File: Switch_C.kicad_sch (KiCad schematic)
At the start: 2 parts

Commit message: progress on CORE pcb
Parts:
- renumbered R801 to R501, R802 to R502
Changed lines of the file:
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@@
 		(on_board yes)
 		(dnp no)
-		(property "Reference" "R801"
+		(property "Reference" "R501"
 			(at 96.52 121.92 0)
 			(effects
@@
 			(project "EPS_CORE"
 				(path "/43e5e7c8-e7e0-4528-9a3e-b1557849918d/170b50a7-486d-470b-9824-bd866624d07a"
-					(reference "R?")
+					(reference "R1501")
 					(unit 1)
 				)
 				(path "/43e5e7c8-e7e0-4528-9a3e-b1557849918d/6ee1dd01-f31d-4eef-845b-d197a7baea1a"
-					(reference "R?")
+					(reference "R1301")
 					(unit 1)
 				)
 				(path "/43e5e7c8-e7e0-4528-9a3e-b1557849918d/7ff03393-ecf4-487d-bab2-a8ed4a4d9be6"
-					(reference "R?")
+					(reference "R701")
 					(unit 1)
 				)
 				(path "/43e5e7c8-e7e0-4528-9a3e-b1557849918d/b6772c72-3c76-48c5-a75b-fb14179eeb30"
-					(reference "R?")
+					(reference "R501")
 					(unit 1)
 				)
@@
 		(on_board yes)
 		(dnp no)
-		(property "Reference" "R802"
+		(property "Reference" "R502"
 			(at 105.41 121.92 0)
 			(effects
@@
 			(project "EPS_CORE"
 				(path "/43e5e7c8-e7e0-4528-9a3e-b1557849918d/170b50a7-486d-470b-9824-bd866624d07a"
-					(reference "R?")
+					(reference "R1502")
 					(unit 1)
 				)
 				(path "/43e5e7c8-e7e0-4528-9a3e-b1557849918d/6ee1dd01-f31d-4eef-845b-d197a7baea1a"
-					(reference "R?")
+					(reference "R1302")
 					(unit 1)
 				)
 				(path "/43e5e7c8-e7e0-4528-9a3e-b1557849918d/7ff03393-ecf4-487d-bab2-a8ed4a4d9be6"
-					(reference "R?")
+					(reference "R702")
 					(unit 1)
 				)
 				(path "/43e5e7c8-e7e0-4528-9a3e-b1557849918d/b6772c72-3c76-48c5-a75b-fb14179eeb30"
-					(reference "R?")
+					(reference "R502")
 					(unit 1)
 				)
@@
 		(dnp no)
 		(fields_autoplaced yes)
-		(property "Reference" "#PWR0165"
+		(property "Reference" "#PWR0164"
 			(at 95.25 132.08 0)
 			(effects
@@
 			(project "EPS_CORE"
 				(path "/43e5e7c8-e7e0-4528-9a3e-b1557849918d/170b50a7-486d-470b-9824-bd866624d07a"
-					(reference "#PWR?")
+					(reference "#PWR0363")
 					(unit 1)
 				)
 				(path "/43e5e7c8-e7e0-4528-9a3e-b1557849918d/6ee1dd01-f31d-4eef-845b-d197a7baea1a"
-					(reference "#PWR?")
+					(reference "#PWR0341")
 					(unit 1)
 				)
 				(path "/43e5e7c8-e7e0-4528-9a3e-b1557849918d/7ff03393-ecf4-487d-bab2-a8ed4a4d9be6"
-					(reference "#PWR?")
+					(reference "#PWR0186")
 					(unit 1)
 				)
 				(path "/43e5e7c8-e7e0-4528-9a3e-b1557849918d/b6772c72-3c76-48c5-a75b-fb14179eeb30"
-					(reference "#PWR?")
+					(reference "#PWR0164")
 					(unit 1)
 				)
@@
 		(dnp no)
 		(fields_autoplaced yes)
-		(property "Reference" "#PWR0166"
+		(property "Reference" "#PWR0165"
 			(at 104.14 132.08 0)
 			(effects
@@
 			(project "EPS_CORE"
 				(path "/43e5e7c8-e7e0-4528-9a3e-b1557849918d/170b50a7-486d-470b-9824-bd866624d07a"
-					(reference "#PWR?")
+					(reference "#PWR0364")
 					(unit 1)
 				)
 				(path "/43e5e7c8-e7e0-4528-9a3e-b1557849918d/6ee1dd01-f31d-4eef-845b-d197a7baea1a"
-					(reference "#PWR?")
+					(reference "#PWR0342")
 					(unit 1)
 				)
 				(path "/43e5e7c8-e7e0-4528-9a3e-b1557849918d/7ff03393-ecf4-487d-bab2-a8ed4a4d9be6"
-					(reference "#PWR?")
+					(reference "#PWR0187")
 					(unit 1)
 				)
 				(path "/43e5e7c8-e7e0-4528-9a3e-b1557849918d/b6772c72-3c76-48c5-a75b-fb14179eeb30"
-					(reference "#PWR?")
-					(unit 1)
-				)
+					(reference "#PWR0165")
+					(unit 1)
+				)

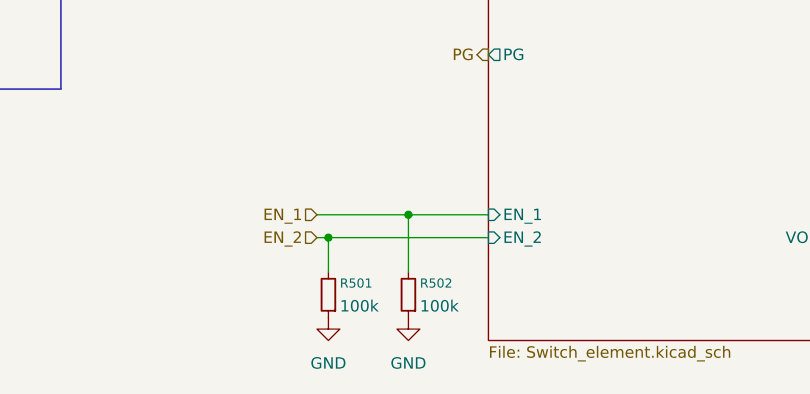
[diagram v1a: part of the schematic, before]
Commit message: pcb progres for all components
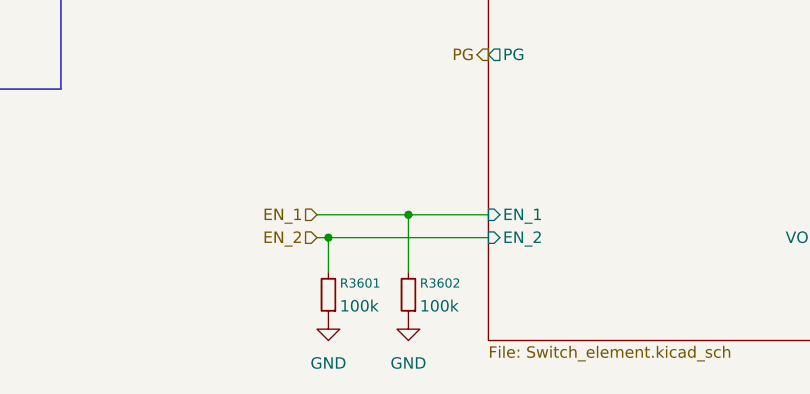
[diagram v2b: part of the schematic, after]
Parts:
- renumbered R501 to R3601, R502 to R3602
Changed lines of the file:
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@@
 		(on_board yes)
 		(dnp no)
-		(property "Reference" "R501"
+		(property "Reference" "R3601"
 			(at 96.52 121.92 0)
 			(effects
@@
 				(path "/94201994-47b8-4213-8d1a-05da12b2a7b0/447ec425-294e-4947-a7f3-941020b4706e/b6772c72-3c76-48c5-a75b-fb14179eeb30"
 					(reference "R5801")
+					(unit 1)
+				)
+			)
+			(project "EPS_OUTPUT_CHANNELS"
+				(path "/c9173887-04ec-4c2a-a5a4-b6a694df57d5/40e3cf3e-b706-4a83-ae9b-eb59be341dee"
+					(reference "R1101")
+					(unit 1)
+				)
+				(path "/c9173887-04ec-4c2a-a5a4-b6a694df57d5/43e909f3-a7d1-4780-9c07-6818bd86e850"
+					(reference "R701")
+					(unit 1)
+				)
+				(path "/c9173887-04ec-4c2a-a5a4-b6a694df57d5/d50b9098-1e1b-4a02-ab50-f7d96145dfa1"
+					(reference "R901")
 					(unit 1)
 				)
@@
 		(on_board yes)
 		(dnp no)
-		(property "Reference" "R502"
+		(property "Reference" "R3602"
 			(at 105.41 121.92 0)
 			(effects
@@
 				(path "/94201994-47b8-4213-8d1a-05da12b2a7b0/447ec425-294e-4947-a7f3-941020b4706e/b6772c72-3c76-48c5-a75b-fb14179eeb30"
 					(reference "R5802")
+					(unit 1)
+				)
+			)
+			(project "EPS_OUTPUT_CHANNELS"
+				(path "/c9173887-04ec-4c2a-a5a4-b6a694df57d5/40e3cf3e-b706-4a83-ae9b-eb59be341dee"
+					(reference "R1102")
+					(unit 1)
+				)
+				(path "/c9173887-04ec-4c2a-a5a4-b6a694df57d5/43e909f3-a7d1-4780-9c07-6818bd86e850"
+					(reference "R702")
+					(unit 1)
+				)
+				(path "/c9173887-04ec-4c2a-a5a4-b6a694df57d5/d50b9098-1e1b-4a02-ab50-f7d96145dfa1"
+					(reference "R902")
 					(unit 1)
 				)
@@
 		(dnp no)
 		(fields_autoplaced yes)
-		(property "Reference" "#PWR0164"
+		(property "Reference" "#PWR03601"
 			(at 95.25 132.08 0)
 			(effects
@@
 				(path "/94201994-47b8-4213-8d1a-05da12b2a7b0/447ec425-294e-4947-a7f3-941020b4706e/b6772c72-3c76-48c5-a75b-fb14179eeb30"
 					(reference "#PWR05801")
+					(unit 1)
+				)
+			)
+			(project "EPS_OUTPUT_CHANNELS"
+				(path "/c9173887-04ec-4c2a-a5a4-b6a694df57d5/40e3cf3e-b706-4a83-ae9b-eb59be341dee"
+					(reference "#PWR01101")
+					(unit 1)
+				)
+				(path "/c9173887-04ec-4c2a-a5a4-b6a694df57d5/43e909f3-a7d1-4780-9c07-6818bd86e850"
+					(reference "#PWR0701")
+					(unit 1)
+				)
+				(path "/c9173887-04ec-4c2a-a5a4-b6a694df57d5/d50b9098-1e1b-4a02-ab50-f7d96145dfa1"
+					(reference "#PWR0901")
 					(unit 1)
 				)
@@
 		(dnp no)
 		(fields_autoplaced yes)
-		(property "Reference" "#PWR0165"
+		(property "Reference" "#PWR03602"
 			(at 104.14 132.08 0)
 			(effects
@@
 					(unit 1)
 				)
+			)
+			(project "EPS_OUTPUT_CHANNELS"
+				(path "/c9173887-04ec-4c2a-a5a4-b6a694df57d5/40e3cf3e-b706-4a83-ae9b-eb59be341dee"
+					(reference "#PWR01102")
+					(unit 1)
+				)
+				(path "/c9173887-04ec-4c2a-a5a4-b6a694df57d5/43e909f3-a7d1-4780-9c07-6818bd86e850"
+					(reference "#PWR0702")
+					(unit 1)
+				)
+				(path "/c9173887-04ec-4c2a-a5a4-b6a694df57d5/d50b9098-1e1b-4a02-ab50-f7d96145dfa1"
+					(reference "#PWR0902")
+					(unit 1)
+				)

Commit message: progress on PCBs
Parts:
- renumbered R3601 to R701, R3602 to R702
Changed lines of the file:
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@@
 		(on_board yes)
 		(dnp no)
-		(property "Reference" "R3601"
+		(property "Reference" "R701"
 			(at 96.52 121.92 0)
 			(effects
@@
 		(on_board yes)
 		(dnp no)
-		(property "Reference" "R3602"
+		(property "Reference" "R702"
 			(at 105.41 121.92 0)
 			(effects
@@
 		(dnp no)
 		(fields_autoplaced yes)
-		(property "Reference" "#PWR03601"
+		(property "Reference" "#PWR0701"
 			(at 95.25 132.08 0)
 			(effects
@@
 		(dnp no)
 		(fields_autoplaced yes)
-		(property "Reference" "#PWR03602"
+		(property "Reference" "#PWR0702"
 			(at 104.14 132.08 0)
 			(effects
